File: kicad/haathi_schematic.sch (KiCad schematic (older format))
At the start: 0 parts

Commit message: Cleanup of top level local labels
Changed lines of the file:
@@
 EESchema Schematic File Version 4
-LIBS:haathi-cache
+LIBS:haathi_schematic-cache
 EELAYER 26 0
 EELAYER END
 $Descr A3 16535 11693
 encoding utf-8
-Sheet 3 11
+Sheet 1 9
 Title "haathi_cam"
 Date "2018-03-11"
@@
 F0 "POWER" 50
 F1 "haathi_power.sch" 50
-F3 "VDD_SNVS_IN" I L 3000 1550 50
-F4 "DCDC_IN" I L 3000 1650 50
-F5 "NVCC_SD0" I R 4450 1550 50
-F6 "NVCC_SD1" I R 4450 1650 50
-F7 "NVCC_EMC" I R 4450 1750 50
-F8 "NVCC_GPIO" I R 4450 1850 50
-F9 "VDDA_ADC_3P3" I L 3000 2050 50
-F10 "VDD_HIGH_IN" I L 3000 1750 50
-F11 "VDD_SNVS_CAP" I R 4450 2050 50
-F12 "VDD_HIGH_CAP" I R 4450 2150 50
-F13 "VDD_SOC_IN" I L 3000 1850 50
-F14 "5V_USB_OTG" I L 3000 2250 50
-F15 "ONOFF" I R 4450 2250 50
-F16 "POR_BUTTON" I R 4450 2350 50
-F17 "WAKEUP_BUTTON" I R 4450 2450 50
+F2 "VDD_SNVS_IN" I L 3000 1550 50
+F3 "DCDC_IN" I L 3000 1650 50
+F4 "NVCC_SD0" I R 4450 1550 50
+F5 "NVCC_SD1" I R 4450 1650 50
+F6 "NVCC_EMC" I R 4450 1750 50
+F7 "NVCC_GPIO" I R 4450 1850 50
+F8 "VDDA_ADC_3P3" I L 3000 2050 50
+F9 "VDD_HIGH_IN" I L 3000 1750 50
+F10 "VDD_SNVS_CAP" I R 4450 2050 50
+F11 "VDD_HIGH_CAP" I R 4450 2150 50
+F12 "VDD_SOC_IN" I L 3000 1850 50
+F13 "5V_USB_OTG" I L 3000 2250 50
+F14 "ONOFF" I R 4450 2250 50
+F15 "POR_BUTTON" I R 4450 2350 50
+F16 "WAKEUP_BUTTON" I R 4450 2450 50
 $EndSheet
 $Sheet
-S 7950 1575 2300 6150
+S 7950 1575 2300 6175
 U 5A6307C3
 F0 "CPU i.MX RT1052" 50
@@
 F94 "5V_USB_HS" I L 7950 6750 50
 F95 "GPIO_B0_04" I R 10250 6450 50
-F96 "GPIO_B0_5" I R 10250 6550 50
-F97 "GPIO_B0_6" I R 10250 6650 50
-F98 "GPIO_B0_7" I R 10250 6750 50
-F99 "GPIO_B0_8" I R 10250 6850 50
-F100 "GPIO_B0_9" I R 10250 6950 50
-F101 "GPIO_B0_10" I R 10250 7050 50
-F102 "GPIO_B0_11" I R 10250 7150 50
-F103 "GPIO_B0_12" I R 10250 7250 50
-F104 "GPIO_B0_13" I R 10250 7350 50
-F105 "GPIO_B0_14" I R 10250 7450 50
-F106 "GPIO_B0_15" I R 10250 7550 50
-F107 "GPIO_AD_B0_04" I R 10250 6250 50
-F108 "GPIO_AD_B0_05" I R 10250 6350 50
-F109 "BACKLIGHT_CTL" I L 7950 7050 50
-F110 "FlexSPI_SS_B" I L 7950 6350 50
-F111 "I2C2_SCL" I R 10250 5650 50
-F112 "I2C2_SDA" I R 10250 5750 50
-F113 "GPIO_AD_B0_00" I R 10250 5850 50
-F114 "GPIO_AD_B0_01" I R 10250 5950 50
-F115 "GPIO_AD_B1_04" I L 7950 7150 50
-F116 "GPIO_AD_B1_05" I L 7950 7250 50
-F117 "GPIO_AD_B1_06" I L 7950 7350 50
-F118 "GPIO_AD_B1_07" I L 7950 7450 50
-F119 "POR_BUTTON" I L 7950 7550 50
+F96 "GPIO_B0_10" I R 10250 7050 50
+F97 "GPIO_B0_11" I R 10250 7150 50
+F98 "GPIO_B0_12" I R 10250 7250 50
+F99 "GPIO_B0_13" I R 10250 7350 50
+F100 "GPIO_B0_14" I R 10250 7450 50
+F101 "GPIO_B0_15" I R 10250 7550 50
+F102 "GPIO_AD_B0_04" I R 10250 6250 50
+F103 "GPIO_AD_B0_05" I R 10250 6350 50
+F104 "BACKLIGHT_CTL" I L 7950 7050 50
+F105 "FlexSPI_SS_B" I L 7950 6350 50
+F106 "I2C2_SCL" I R 10250 5650 50
+F107 "I2C2_SDA" I R 10250 5750 50
+F108 "GPIO_AD_B0_00" I R 10250 5850 50
+F109 "GPIO_AD_B0_01" I R 10250 5950 50
+F110 "GPIO_AD_B1_04" I L 7950 7150 50
+F111 "GPIO_AD_B1_05" I L 7950 7250 50
+F112 "GPIO_AD_B1_06" I L 7950 7350 50
+F113 "GPIO_AD_B1_07" I L 7950 7450 50
+F114 "POR_BUTTON" I L 7950 7550 50
+F115 "GPIO_B0_05" I R 10250 6550 50
+F116 "GPIO_B0_06" I R 10250 6650 50
+F117 "GPIO_B0_07" I R 10250 6750 50
+F118 "GPIO_B0_08" I R 10250 6850 50
+F119 "GPIO_B0_09" I R 10250 6950 50
+F120 "MCU_RESET_N" I L 7950 7650 50
+F121 "DCDC_IN" I R 10250 7650 50
 $EndSheet
 $Sheet
@@
 F0 "INTERFACES GPIO JTAG" 50
 F1 "haathi_interfaces.sch" 50
-F2 "LED_R" I L 12500 1650 50
-F3 "LED_G" I L 12500 1750 50
-F4 "LED_B" I L 12500 1850 50
-F5 "USER_SW_0" I L 12500 1950 50
-F6 "USER_SW_1" I L 12500 2050 50
 F7 "JTAG_nTRST" I L 12500 2150 50
 F8 "JTAG_TCK" I L 12500 2250 50
@@
 $EndSheet
 $Sheet
-S 12500 5075 2050 575
+S 12500 5075 2050 775
 U 5A6308E9
 F0 "SD RAM" 50
@@
 F3 "SEMC_D[0..7]" I L 12500 5250 50
 F4 "SEMC_D[8..15]" I L 12500 5350 50
-F5 "DCDC_IN" I L 12500 5450 50
+F5 "SEMC_BA0" I R 14550 5150 50
+F6 "SEMC_BA1" I R 14550 5250 50
+F7 "SEMC_RAS" I R 14550 5350 50
+F8 "SEMC_CAS" I R 14550 5450 50
+F9 "SEMC_WE" I R 14550 5550 50
+F10 "SEMC_CS0" I R 14550 5650 50
+F11 "SEMC_DM0" I L 12500 5550 50
+F12 "SEMC_DM1" I L 12500 5650 50
+F13 "SEMC_CLK" I L 12500 5450 50
+F14 "SEMC_CKE" I R 14550 5750 50
 $EndSheet
 $Sheet
@@
 F0 "CSI CAMERA" 50
 F1 "haathi_camera.sch" 50
-F18 "I2C1_SCL" I L 3050 5600 50
-F19 "I2C1_SDA" I L 3050 5500 50
-F22 "GPIO_AD_B1_04" I R 4500 4500 50
-F23 "GPIO_AD_B1_05" I R 4500 4600 50
-F24 "GPIO_AD_B1_06" I R 4500 4700 50
-F25 "GPIO_AD_B1_07" I R 4500 4800 50
-F26 "GPIO_AD_B1_10" I R 4500 5100 50
-F27 "GPIO_AD_B1_11" I R 4500 5200 50
-F28 "GPIO_AD_B1_12" I R 4500 5300 50
-F29 "GPIO_AD_B1_13" I R 4500 5400 50
-F30 "GPIO_AD_B1_14" I R 4500 5500 50
-F31 "GPIO_AD_B1_15" I R 4500 5600 50
-F32 "GPIO_B1_11" I L 3050 4800 50
-F33 "GPIO_B1_10" I L 3050 4700 50
-F36 "GPIO_AD_B1_09" I R 4500 5000 50
-F37 "GPIO_AD_B1_08" I R 4500 4900 50
-F38 "GPIO_B1_09" I L 3050 4600 50
-F42 "GPIO_B1_08" I L 3050 4500 50
-F43 "GPIO_EMC_33" I L 3050 5300 50
-F44 "GPIO_EMC_32" I L 3050 5200 50
-F45 "GPIO_EMC_31" I L 3050 5100 50
-F46 "GPIO_EMC_30" I L 3050 5000 50
+F2 "I2C1_SCL" I L 3050 5600 50
+F3 "I2C1_SDA" I L 3050 5500 50
+F4 "GPIO_AD_B1_04" I R 4500 4500 50
+F5 "GPIO_AD_B1_05" I R 4500 4600 50
+F6 "GPIO_AD_B1_06" I R 4500 4700 50
+F7 "GPIO_AD_B1_07" I R 4500 4800 50
+F8 "GPIO_AD_B1_10" I R 4500 5100 50
+F9 "GPIO_AD_B1_11" I R 4500 5200 50
+F10 "GPIO_AD_B1_12" I R 4500 5300 50
+F11 "GPIO_AD_B1_13" I R 4500 5400 50
+F12 "GPIO_AD_B1_14" I R 4500 5500 50
+F13 "GPIO_AD_B1_15" I R 4500 5600 50
+F14 "GPIO_B1_11" I L 3050 4800 50
+F15 "GPIO_B1_10" I L 3050 4700 50
+F16 "GPIO_AD_B1_09" I R 4500 5000 50
+F17 "GPIO_AD_B1_08" I R 4500 4900 50
+F18 "GPIO_B1_09" I L 3050 4600 50
+F19 "GPIO_B1_08" I L 3050 4500 50
+F20 "GPIO_EMC_33" I L 3050 5300 50
+F21 "GPIO_EMC_32" I L 3050 5200 50
+F22 "GPIO_EMC_31" I L 3050 5100 50
+F23 "GPIO_EMC_30" I L 3050 5000 50
 $EndSheet
 $Sheet
-S 12500 6150 2050 800
+S 12500 6200 2050 800
 U 5A630933
 F0 "MISC JUMPERS" 50
@@
 Wire Wire Line
 	10250 6450 10850 6450
-Wire Wire Line
-	10250 6550 10850 6550
-Wire Wire Line
-	10250 6650 10850 6650
-Wire Wire Line
-	10250 6750 10850 6750
-Wire Wire Line
-	10250 6850 10850 6850
-Wire Wire Line
-	10250 6950 10850 6950
 Wire Wire Line
 	10250 7050 10850 7050
@@
 Text Label 10850 6450 2    50   ~ 0
 GPIO_B0_04
-Text Label 10850 6550 2    50   ~ 0
-GPIO_B0_05
-Text Label 10850 6650 2    50   ~ 0
-GPIO_B0_06
-Text Label 10850 6750 2    50   ~ 0
-GPIO_B0_07
-Text Label 10850 6850 2    50   ~ 0
-GPIO_B0_08
-Text Label 10850 6950 2    50   ~ 0
-GPIO_B0_09
 Text Label 10850 7050 2    50   ~ 0
 GPIO_B0_10
@@
 GPIO_B0_15
 Wire Wire Line
-	11800 1750 12500 1750
-Wire Wire Line
-	11800 1850 12500 1850
-Wire Wire Line
-	11800 1950 12500 1950
-Wire Wire Line
-	11800 2050 12500 2050
-Wire Wire Line
 	11800 2150 12500 2150
 Wire Wire Line
@@
 Wire Wire Line
 	11800 4650 12500 4650
-Wire Wire Line
-	11800 1650 12500 1650
-Text Label 11800 1650 0    50   ~ 0
-LED_R
-Text Label 11800 1750 0    50   ~ 0
-LED_G
-Text Label 11800 1850 0    50   ~ 0
-LED_B
-Text Label 11800 1950 0    50   ~ 0
-USER_SW_0
-Text Label 11800 2050 0    50   ~ 0
-USER_SW_1
 Text Label 11800 2150 0    50   ~ 0
 JTAG_nTRST
@@
 Wire Bus Line
 	12500 5350 11800 5350
-Wire Wire Line
-	12500 5450 12000 5450
 Text Label 11800 5150 0    50   ~ 0
 SEMC_A[0..12]
@@
 Text Label 11800 5350 0    50   ~ 0
 SEMC_D[8..15]
-Text Label 12000 5450 0    50   ~ 0
-DCDC_IN
 Wire Wire Line
 	2975 3650 2350 3650
@@
 Text Label 2350 2250 0    50   ~ 0
 5V_USB_OTG
+Wire Wire Line
+	10250 7650 10850 7650
+Text Label 10850 7650 2    50   ~ 0
+DCDC_IN
+Wire Wire Line
+	7950 7650 7100 7650
+Text Label 7100 7650 0    50   ~ 0
+MCU_RESET_N
+Wire Wire Line
+	10250 6550 10850 6550
+Wire Wire Line
+	10250 6650 10850 6650
+Wire Wire Line
+	10250 6750 10850 6750
+Wire Wire Line
+	10250 6850 10850 6850
+Wire Wire Line
+	10250 6950 10850 6950
+Text Label 10850 6550 2    50   ~ 0
+GPIO_B0_05
+Text Label 10850 6650 2    50   ~ 0
+GPIO_B0_06
+Text Label 10850 6750 2    50   ~ 0
+GPIO_B0_07
+Text Label 10850 6850 2    50   ~ 0
+GPIO_B0_08
+Text Label 10850 6950 2    50   ~ 0
+GPIO_B0_09
+Wire Wire Line
+	12500 5450 11800 5450
+Wire Wire Line
+	12500 5550 11800 5550
+Wire Wire Line
+	12500 5650 11800 5650
+Wire Wire Line
+	14550 5150 15200 5150
+Wire Wire Line
+	14550 5250 15200 5250
+Wire Wire Line
+	14550 5350 15200 5350
+Wire Wire Line
+	14550 5450 15200 5450
+Wire Wire Line
+	14550 5550 15200 5550
+Wire Wire Line
+	14550 5650 15200 5650
+Wire Wire Line
+	14550 5750 15200 5750
+Text Label 11800 5450 0    50   ~ 0
+SEMC_CLK
+Text Label 11800 5550 0    50   ~ 0
+SEMC_DM0
+Text Label 11800 5650 0    50   ~ 0
+SEMC_DM1
+Text Label 15200 5150 2    50   ~ 0
+SEMC_BA0
+Text Label 15200 5250 2    50   ~ 0
+SEMC_BA1
+Text Label 15200 5350 2    50   ~ 0
+SEMC_RAS
+Text Label 15200 5450 2    50   ~ 0
+SEMC_CAS
+Text Label 15200 5550 2    50   ~ 0
+SEMC_WE
+Text Label 15200 5650 2    50   ~ 0
+SEMC_CS0
+Text Label 15200 5750 2    50   ~ 0
+SEMC_CKE
 $EndSCHEMATC

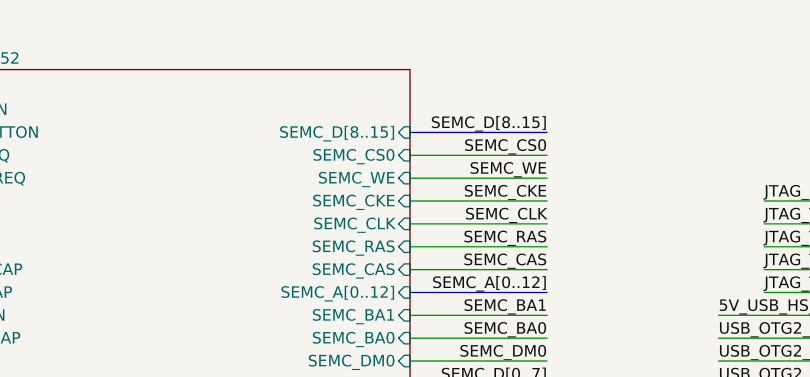
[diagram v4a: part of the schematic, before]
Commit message: USB_OTG1_ID and USB_OTG2_ID pins: Add to CPU sheet
Add configurability on the way these pins can be used, using 0R
resistors.

Signed-off-by: Kumar Abhishek <abhishek@theembeddedkitchen.net>
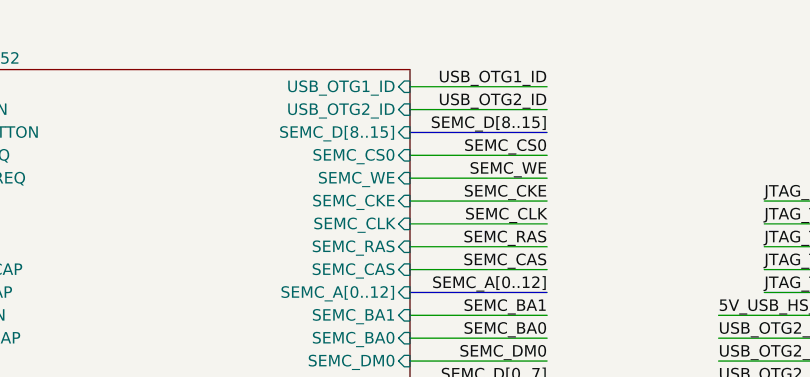
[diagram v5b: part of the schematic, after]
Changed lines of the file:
@@
 EESchema Schematic File Version 4
-LIBS:haathi_schematic-cache
 EELAYER 26 0
 EELAYER END
@@
 F120 "MCU_RESET_N" I L 7950 7650 50
 F121 "DCDC_IN" I R 10250 7650 50
+F122 "USB_OTG1_ID" I R 10250 1650 50
+F123 "USB_OTG2_ID" I R 10250 1750 50
 $EndSheet
 $Sheet
@@
 F0 "INTERFACES GPIO JTAG" 50
 F1 "haathi_interfaces.sch" 50
-F7 "JTAG_nTRST" I L 12500 2150 50
-F8 "JTAG_TCK" I L 12500 2250 50
-F9 "JTAG_TMS" I L 12500 2350 50
-F10 "JTAG_TDO" I L 12500 2450 50
-F11 "JTAG_TDI" I L 12500 2550 50
-F12 "5V_USB_HS_EXTERN" I L 12500 2650 50
-F13 "USB_OTG2_D-_EXTERN" I L 12500 2750 50
-F14 "USB_OTG2_D+_EXTERN" I L 12500 2850 50
-F15 "USB_OTG2_ID_EXTERN" I L 12500 2950 50
-F16 "USB_GND_EXTERN" I L 12500 3050 50
-F17 "ONOFF" I L 12500 3350 50
-F18 "WAKEUP_BUTTON" I L 12500 3250 50
-F19 "5V_USB_OTG" I L 12500 3150 50
-F20 "I2C1_SCL" I L 12500 3450 50
-F21 "I2C1_SDA" I L 12500 3550 50
-F22 "UART1_TXD" I L 12500 3650 50
-F23 "UART1_RXD" I L 12500 3750 50
-F24 "FlexSPI_D0_B" I R 14550 4150 50
-F25 "FlexSPI_D1_B" I R 14550 4250 50
-F26 "FlexSPI_CLK_B" I R 14550 4050 50
-F27 "FlexSPI_SS_B" I R 14550 3950 50
-F28 "SAI1_MCLK" I R 14550 3850 50
-F29 "AUD_INT" I R 14550 3750 50
-F30 "SAI1_RX_SYNC" I R 14550 3650 50
-F31 "SAI1_RX_BCLK" I R 14550 3550 50
-F32 "SAI1_RXD" I R 14550 3450 50
-F33 "SAI1_TXD" I R 14550 3350 50
-F34 "SAI1_TX_BCLK" I R 14550 3250 50
-F35 "SAI1_TX_SYNC" I R 14550 3150 50
-F36 "CAN2_TX" I R 14550 3050 50
-F37 "CAN2_RX" I R 14550 2950 50
-F38 "LCDIF_D[0..15]" I R 14550 2850 50
-F39 "LCDIF_CLK" I R 14550 2750 50
-F40 "LCDIF_ENABLE" I R 14550 2650 50
-F41 "LCDIF_HSYNC" I R 14550 2550 50
-F42 "LCDIF_VSYNC" I R 14550 2450 50
-F43 "ENET_CRS_DV" I R 14550 2350 50
-F44 "ENET_RXD0" I R 14550 2250 50
-F45 "ENET_TXD0" I R 14550 2150 50
-F46 "BACKLIGHT_CTL" I R 14550 2050 50
-F47 "ENET_RXD1" I R 14550 1950 50
-F48 "ENET_TXD1" I R 14550 1850 50
-F49 "ENET_TXEN" I R 14550 1750 50
-F50 "ENET_TX_CLK" I R 14550 1650 50
-F51 "ENET_RXER" I L 12500 4050 50
-F52 "I2C2_SCL" I L 12500 3850 50
-F53 "I2C2_SDA" I L 12500 3950 50
-F54 "GPIO_AD_B0_00" I L 12500 4150 50
-F55 "GPIO_AD_B0_01" I L 12500 4250 50
-F56 "GPIO_AD_B1_04" I L 12500 4350 50
-F57 "GPIO_AD_B1_05" I L 12500 4450 50
-F58 "GPIO_AD_B1_06" I L 12500 4550 50
-F59 "GPIO_AD_B1_07" I L 12500 4650 50
-F60 "FlexSPI_D2_B" I R 14550 4350 50
-F61 "FlexSPI_D3_B" I R 14550 4450 50
-F62 "SPDIF_IN" I R 14550 4550 50
-F63 "SPDIF_OUT" I R 14550 4650 50
+F2 "JTAG_nTRST" I L 12500 2150 50
+F3 "JTAG_TCK" I L 12500 2250 50
+F4 "JTAG_TMS" I L 12500 2350 50
+F5 "JTAG_TDO" I L 12500 2450 50
+F6 "JTAG_TDI" I L 12500 2550 50
+F7 "5V_USB_HS_EXTERN" I L 12500 2650 50
+F8 "USB_OTG2_D-_EXTERN" I L 12500 2750 50
+F9 "USB_OTG2_D+_EXTERN" I L 12500 2850 50
+F10 "USB_OTG2_ID_EXTERN" I L 12500 2950 50
+F11 "USB_GND_EXTERN" I L 12500 3050 50
+F12 "ONOFF" I L 12500 3350 50
+F13 "WAKEUP_BUTTON" I L 12500 3250 50
+F14 "5V_USB_OTG" I L 12500 3150 50
+F15 "I2C1_SCL" I L 12500 3450 50
+F16 "I2C1_SDA" I L 12500 3550 50
+F17 "UART1_TXD" I L 12500 3650 50
+F18 "UART1_RXD" I L 12500 3750 50
+F19 "FlexSPI_D0_B" I R 14550 4150 50
+F20 "FlexSPI_D1_B" I R 14550 4250 50
+F21 "FlexSPI_CLK_B" I R 14550 4050 50
+F22 "FlexSPI_SS_B" I R 14550 3950 50
+F23 "SAI1_MCLK" I R 14550 3850 50
+F24 "AUD_INT" I R 14550 3750 50
+F25 "SAI1_RX_SYNC" I R 14550 3650 50
+F26 "SAI1_RX_BCLK" I R 14550 3550 50
+F27 "SAI1_RXD" I R 14550 3450 50
+F28 "SAI1_TXD" I R 14550 3350 50
+F29 "SAI1_TX_BCLK" I R 14550 3250 50
+F30 "SAI1_TX_SYNC" I R 14550 3150 50
+F31 "CAN2_TX" I R 14550 3050 50
+F32 "CAN2_RX" I R 14550 2950 50
+F33 "LCDIF_D[0..15]" I R 14550 2850 50
+F34 "LCDIF_CLK" I R 14550 2750 50
+F35 "LCDIF_ENABLE" I R 14550 2650 50
+F36 "LCDIF_HSYNC" I R 14550 2550 50
+F37 "LCDIF_VSYNC" I R 14550 2450 50
+F38 "ENET_CRS_DV" I R 14550 2350 50
+F39 "ENET_RXD0" I R 14550 2250 50
+F40 "ENET_TXD0" I R 14550 2150 50
+F41 "BACKLIGHT_CTL" I R 14550 2050 50
+F42 "ENET_RXD1" I R 14550 1950 50
+F43 "ENET_TXD1" I R 14550 1850 50
+F44 "ENET_TXEN" I R 14550 1750 50
+F45 "ENET_TX_CLK" I R 14550 1650 50
+F46 "ENET_RXER" I L 12500 4050 50
+F47 "I2C2_SCL" I L 12500 3850 50
+F48 "I2C2_SDA" I L 12500 3950 50
+F49 "GPIO_AD_B0_00" I L 12500 4150 50
+F50 "GPIO_AD_B0_01" I L 12500 4250 50
+F51 "GPIO_AD_B1_04" I L 12500 4350 50
+F52 "GPIO_AD_B1_05" I L 12500 4450 50
+F53 "GPIO_AD_B1_06" I L 12500 4550 50
+F54 "GPIO_AD_B1_07" I L 12500 4650 50
+F55 "FlexSPI_D2_B" I R 14550 4350 50
+F56 "FlexSPI_D3_B" I R 14550 4450 50
+F57 "SPDIF_IN" I R 14550 4550 50
+F58 "SPDIF_OUT" I R 14550 4650 50
 $EndSheet
 $Sheet
@@
 Text Label 15200 5750 2    50   ~ 0
 SEMC_CKE
+Wire Wire Line
+	10250 1750 10850 1750
+Wire Wire Line
+	10250 1650 10850 1650
+Text Label 10850 1650 2    50   ~ 0
+USB_OTG1_ID
+Text Label 10850 1750 2    50   ~ 0
+USB_OTG2_ID
 $EndSCHEMATC
